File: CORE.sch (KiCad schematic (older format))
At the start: 25 parts

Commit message: corrected CAN schematic
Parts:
- added R5: 22, Resistor_SMD:R_0603_1608Metric, symbol Device:R
- C1: renamed from C?; Description 10nF ±10% 50V X7R 0805 Multilayer Ceramic Capacitors -> 10nF ±10% 50V X7R 1206 Multilayer Ceramic Capacitors; Mount (none) -> MOUNT; MountType (none) -> SMD; PartNumber (none) -> CL31B103KBCNNNC
- C2, C3: renamed from C?; Mount (none) -> MOUNT; MountType (none) -> SMD
- C4, C5, C6, C7, C8, C9: renamed from C?; footprint Capacitor_SMD:C_0805_2012Metric -> Capacitor_SMD:C_0603_1608Metric; Description 100nF ±10% 50V X7R 0805 Multilayer Ceramic Capacitors -> 100nF ±10% 100V X7R 0603 Multilayer Ceramic Capacitors; Mount (none) -> MOUNT; MountType (none) -> SMD; PartNumber CL21B104KBCNNNC -> CL10B104KC8NNNC
- D1: renamed from D?; value LED -> LED GREEN; footprint (none) -> LED_SMD:LED_0805_2012Metric; Description (none) -> Green 567.5~576.5nm 0805 Light Emitting Diodes (LED) RoHS; Manufacturer (none) -> Lite-On; Mount (none) -> MOUNT; MountType (none) -> SMD; PartNumber (none) -> LTST-C170KGKT
- D2: renamed from D?; value LED -> LED RED; footprint (none) -> LED_SMD:LED_0805_2012Metric; Description (none) -> Red 631~639nm 0805 Light Emitting Diodes (LED) RoHS; Manufacturer (none) -> Lite-On; Mount (none) -> MOUNT; MountType (none) -> SMD; PartNumber (none) -> LTST-C170KRKT
- D3: renamed from D?; value LED -> LED ORANGE; footprint (none) -> LED_SMD:LED_0805_2012Metric; Description (none) -> Orange 605nm 0805 Light Emitting Diodes (LED) RoHS; Manufacturer (none) -> Lite-On; Mount (none) -> MOUNT; MountType (none) -> SMD; PartNumber (none) -> LTST-C171KFKT
- J3: renamed from J?; Mount (none) -> DO NOT MOUNT; MountType (none) -> TH
- R1, R10, R6, R7, R8, R9: renamed from R?; Mount (none) -> MOUNT; MountType (none) -> SMD
- R2, R3, R4: renamed from R?; Description 680 ±1% 1/10W ±100ppm/°C 0603 Chip Resistor - Surface Mount -> 680Ω ±1% 0.1W ±100ppm/℃ 0603 Chip Resistor - Surface Mount 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; Manufacturer (none) -> YAGEO; Mount (none) -> MOUNT; MountType (none) -> SMD; PartNumber (none) -> RC0603FR-07680RL
- SW1: renamed from SW?; Mount (none) -> MOUNT; MountType (none) -> SMD
- U1: renamed from U?; Description (none) -> 32-Bit ARM® Cortex®-M3 72MHz, FLASH 128kB, RAM 64kB, 2V ~ 3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; Manufacturer (none) -> ST Microelectronics; Mount (none) -> MOUNT; MountType (none) -> SMD; PartNumber (none) -> STM32F105RBT6
- ZQ1: renamed from ZQ?; value 12MHz -> 8MHz; Mount (none) -> MOUNT; MountType (none) -> SMD
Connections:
- net HFQ2: now also R5.1; no longer C3.1, ZQ1.3
- new net: C3.1, R5.2, ZQ1.3

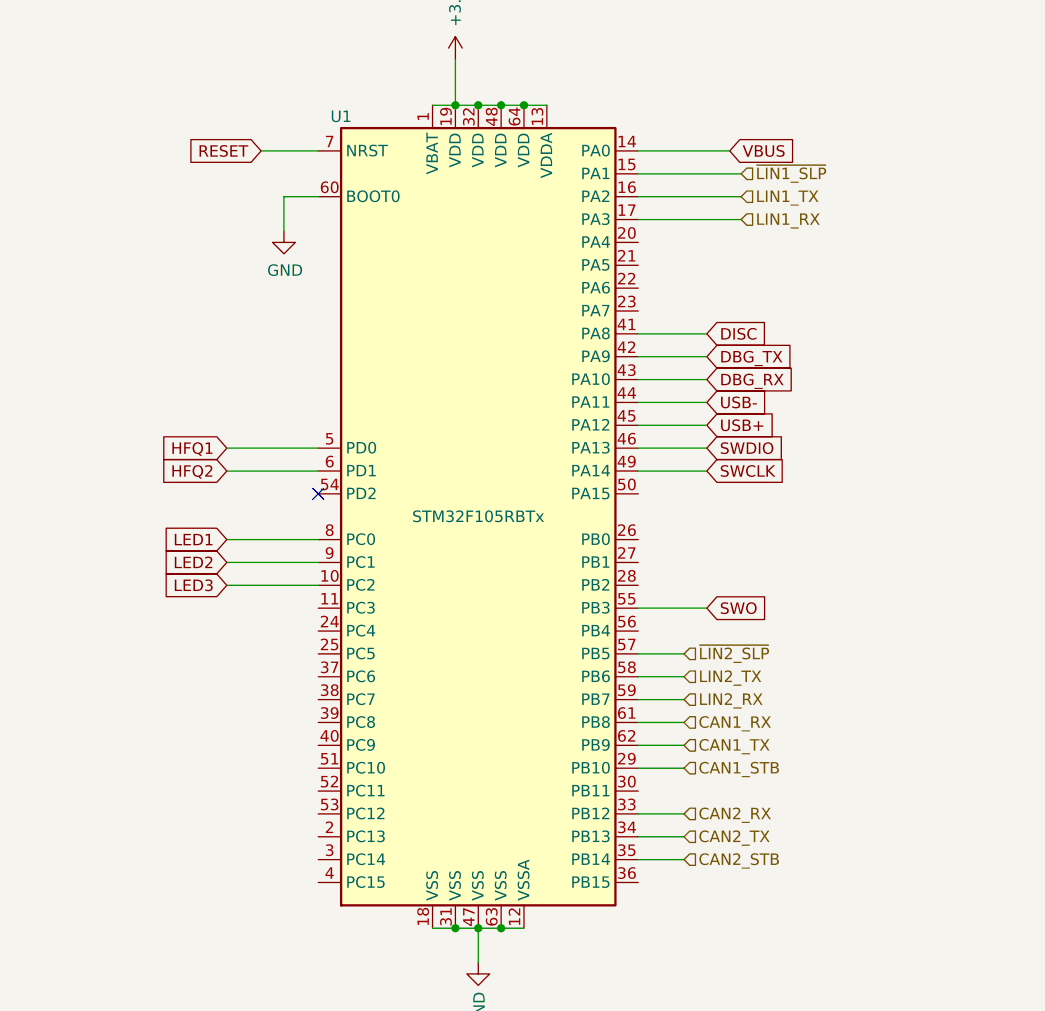
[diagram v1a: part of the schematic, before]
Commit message: CAN part routing
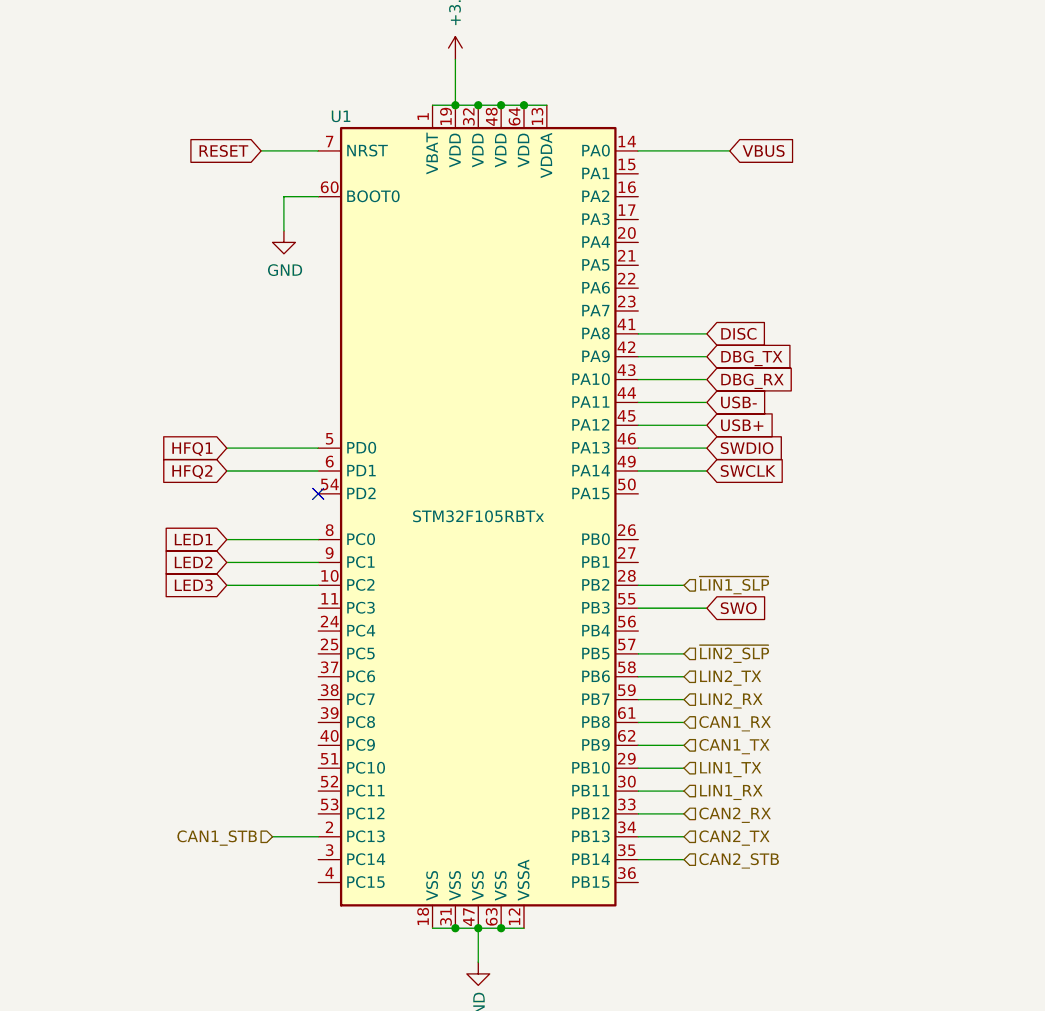
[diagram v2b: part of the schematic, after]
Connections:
- net CAN1_STB: now also U1.2 (PC13); no longer U1.29 (PB10)
- net LIN1_RX: now also U1.30 (PB11); no longer U1.17 (PA3)
- net LIN1_TX: now also U1.29 (PB10); no longer U1.16 (PA2)
- net ~LIN1_SLP: now also U1.28 (PB2); no longer U1.15 (PA1)
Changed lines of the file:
@@
 Text HLabel 6550 4950 2    50   Input ~ 0
 CAN2_STB
-Text HLabel 6550 4550 2    50   Input ~ 0
+Text HLabel 4750 4850 0    50   Input ~ 0
 CAN1_STB
 Wire Wire Line
@@
 EndData
 $EndBitmap
-Text HLabel 6800 2050 2    50   Input ~ 0
+Text HLabel 6550 4550 2    50   Input ~ 0
 LIN1_TX
-Text HLabel 6800 2150 2    50   Input ~ 0
+Text HLabel 6550 4650 2    50   Input ~ 0
 LIN1_RX
 Text HLabel 6550 4150 2    50   Input ~ 0
@@
 Text HLabel 6550 4250 2    50   Input ~ 0
 LIN2_RX
-Text HLabel 6800 1950 2    50   Input ~ 0
+Text HLabel 6550 3750 2    50   Input ~ 0
 ~LIN1_SLP
 Text HLabel 6550 4050 2    50   Input ~ 0
 ~LIN2_SLP
 Wire Wire Line
-	6350 2050 6800 2050
+	6350 4550 6550 4550
 Wire Wire Line
-	6350 2150 6800 2150
+	6350 4650 6550 4650
 Wire Wire Line
-	6800 1950 6350 1950
+	6550 3750 6350 3750
 Wire Wire Line
 	9150 5900 9400 5900
@@
 	6350 4450 6550 4450
 Wire Wire Line
-	6550 4550 6350 4550
+	4750 4850 4950 4850
 Text GLabel 2350 4000 2    50   Input ~ 0
 LED1
